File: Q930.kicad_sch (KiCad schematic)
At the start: 2 parts, among them U1 MW-R-WX

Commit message: continue
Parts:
- added C1, C2, C3: 0.1u, symbol Device:C_Small
- added J1: 7Pin, symbol Connector:Conn_01x07_Socket
- added LED1: LB Q39E-L2OO-35-1, LED_LBQ39E_OSR, symbol q930:LB_Q39E-L2OO-35-1
- added R1, R2: 3.3k, symbol Device:R_US
- added R3: 470, symbol Device:R_US
- added R4: 27k, symbol Device:R_US
- added U2: DRV5032FDDMRR, DMR0004A, symbol q930:DRV5032FDDMRR
- added U3: SHT40I-AD1B-R2, SHT40I_SEN, symbol q930:SHT40I-AD1B-R2
- added U4: TPL5010DDCR, DDC0006A_N, symbol q930:TPL5010DDCR
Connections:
- net GND: now also C1.2, C2.1, C3.2, J1.1 (Pin_1), U2.2 (GND), U3.4 (VSS), U4.2 (GND)
- net +3V0: now reaches BT1.1 (+), U1.5 (VCC)
- net +3V0: now also C1.1, C2.2, C3.1, J1.6 (Pin_6), R1.1, R2.1, R3.1, R4.1, U2.1 (VCC), U3.3 (VDD), U4.1 (VDD)
- net W_SCL: now reaches U1.14 (DIO14/SCL)
- net W_SCL: now also R1.2, U3.2 (SCL)
- net W_SDA: now reaches U1.17 (DIO15/SDA)
- net W_SDA: now also R2.2, U3.1 (SDA)
- net at U1.2 (DO1/PWM3): now also J1.3 (Pin_3)
- net at U1.21 (~{RESET}): now also J1.5 (Pin_5)
- net LED: now reaches U1.7 (DIO5/PWM1)
- net LED: now also LED1.1
- net at U1.8 (DIO6/TX): now also J1.2 (Pin_2)
- net at U1.9 (DIO7/RX): now also J1.4 (Pin_4)
- new net: LED1.2, R3.2
- new net: R4.2, U4.3 (DELAY_M_RST)
- new net SNS_OUT1: U2.4 (OUT)
- new net SNS_OUT2: U2.3 (OUT2)
- no-connect marks 0 -> 1

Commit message: 途中
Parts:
- added D1: 1SS387CT_L3FT, CST2_TOS, symbol q930:1SS387CT_L3FT
- C1, C2, C3: footprint (none) -> Capacitor_SMD:C_0603_1608Metric_Pad1.08x0.95mm_HandSolder
- R1, R2, R3, R4: footprint (none) -> Resistor_SMD:R_0201_0603Metric_Pad0.64x0.40mm_HandSolder
- U4: footprint DDC0006A_N -> q930:DDC0006A_L
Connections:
- net RESETN: now reaches J1.5 (Pin_5), U1.21 (~{RESET})
- net RESETN: now also D1.2
- net WDTOUT: now reaches U4.4 (DONE)
- net WDTOUT: now also U1.15 (DIO13/DI2)
- net at U4.6 (RST_N): now also D1.1
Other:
- moved on the sheet: C3

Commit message: 途中
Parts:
- added U5: SEN-14480, q930:SEN-14480, symbol q930:SEN-14480
- BT1: value Battery_Cell -> CR2032
- J1: footprint (none) -> Connector_PinSocket_2.54mm:PinSocket_1x07_P2.54mm_Vertical_SMD_Pin1Left
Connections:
- net +3V0: now also U5.6 (Vcc)
- net GND: now also U5.5 (GND)
- net SNS_OUT1: now also U1.18 (DIO16/DI4)
- net SNS_OUT2: now also U1.10 (DIO8/PWM4)
- net W_SCL: now also U5.8 (SCL)
- net W_SDA: now also U5.7 (SDA)
- net TX: now reaches J1.2 (Pin_2), U1.8 (DIO6/TX)
- net SPIMISO: now reaches J1.3 (Pin_3), U1.2 (DO1/PWM3)
- net RX: now reaches J1.4 (Pin_4), U1.9 (DIO7/RX)
- net at J1.7 (Pin_7): now also U1.13 (DIO12/DI1)
- net INT1: now reaches U1.24 (DIO0/AI2)
- net INT1: now also U5.4 (INT1)
- net INT2: now reaches U1.25 (DIO1/AI4)
- net INT2: now also U5.3 (INT2)
- no-connect marks 1 -> 4
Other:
- moved on the sheet: BT1, C1

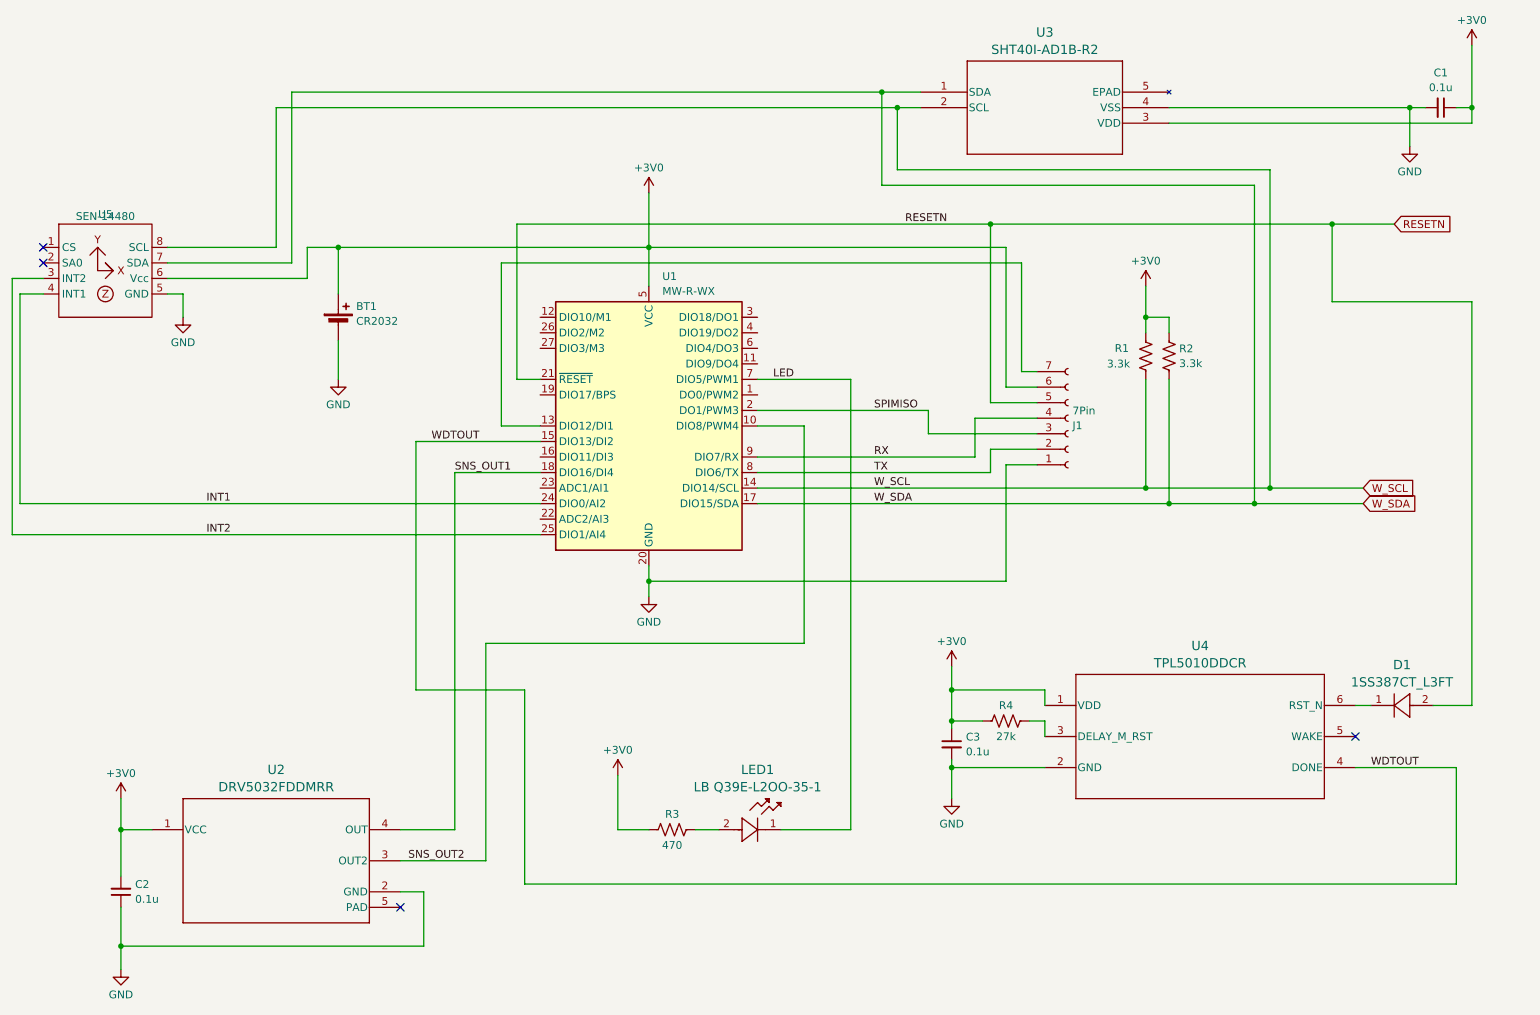
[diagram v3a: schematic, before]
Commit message: シンボル整形
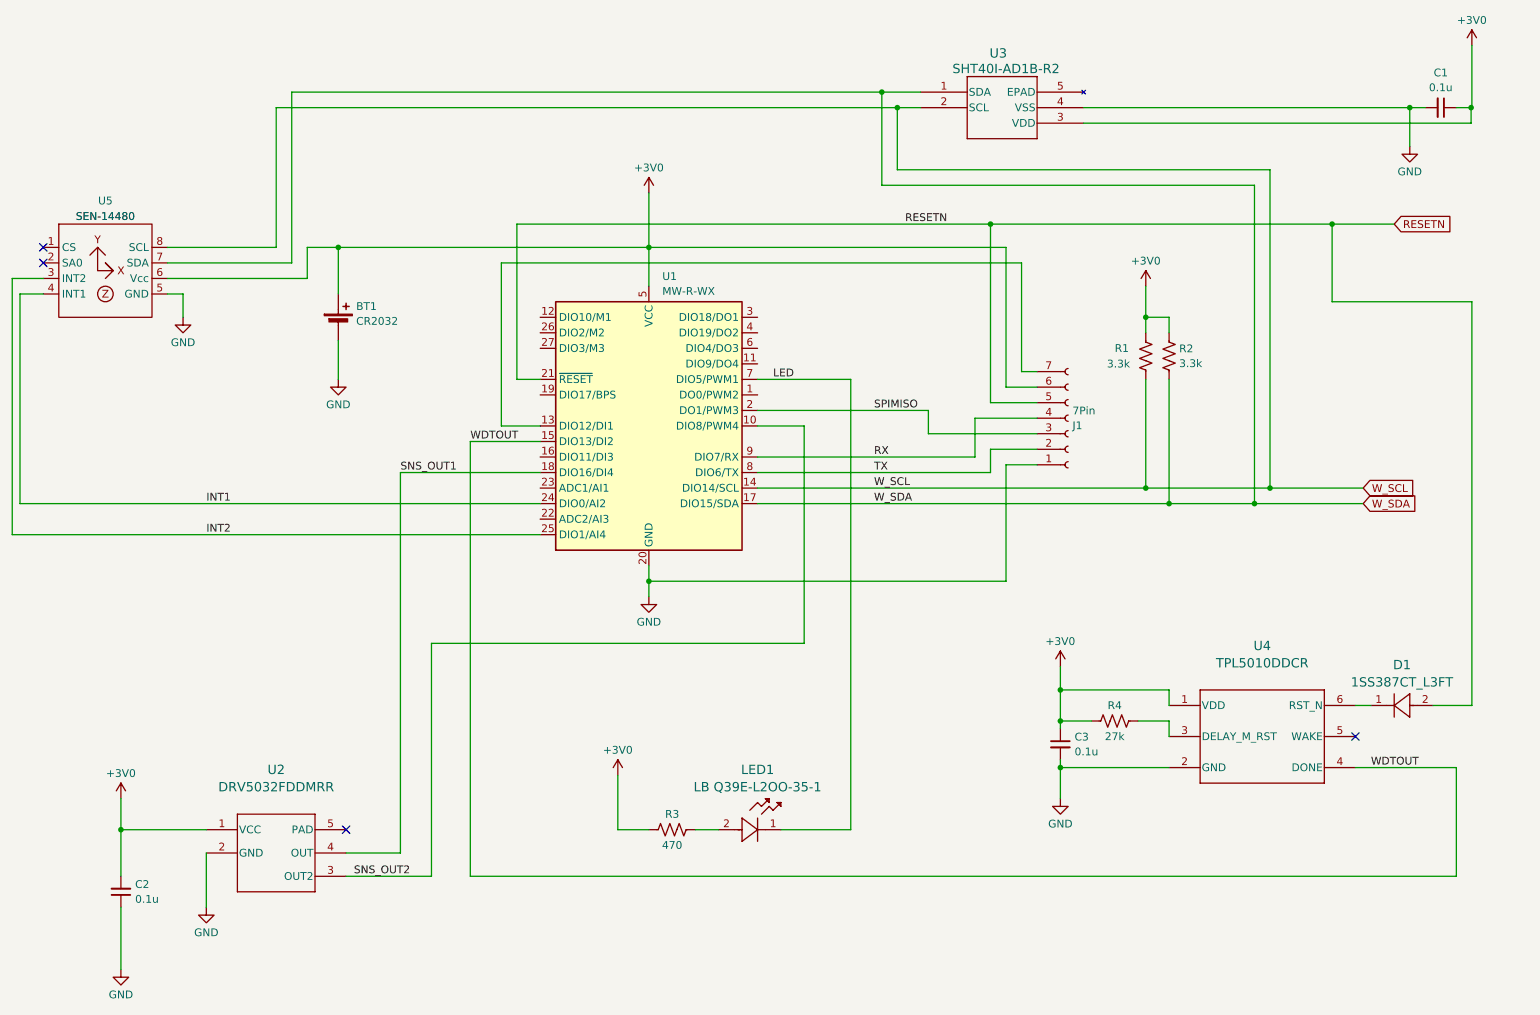
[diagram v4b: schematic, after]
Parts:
- U4: footprint q930:DDC0006A_L -> DDC0006A_N
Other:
- company: (none) -> YS Lab
- title: (none) -> Minisize TWE sensor proto
- moved on the sheet: C3, R4, U2, U3, U4
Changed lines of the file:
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@@
 (kicad_sch (version 20230121) (generator eeschema)
   (paper "A4")
+  (title_block
+    (title "Minisize TWE sensor proto")
+    (date "2024-01-30")
+    (rev "1.00")
+    (company "YS Lab")
+  )
